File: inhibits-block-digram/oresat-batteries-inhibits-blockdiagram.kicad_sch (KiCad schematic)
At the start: 20 parts, among them J1 RBF, J2 RBF TAG, Q1 Q_NMOS, Q2 Q_PMOS, Q3 Q_PMOS, Q4 Q_PMOS, Q6 Q_PMOS, SW1 NEG BATTERY DISCONNECT, SW2 POSITIVE BATTERY DISCONNECT 1, SW3 POSITIVE BATT DISC 2, SW4 POSITIVE BATT DISC 3

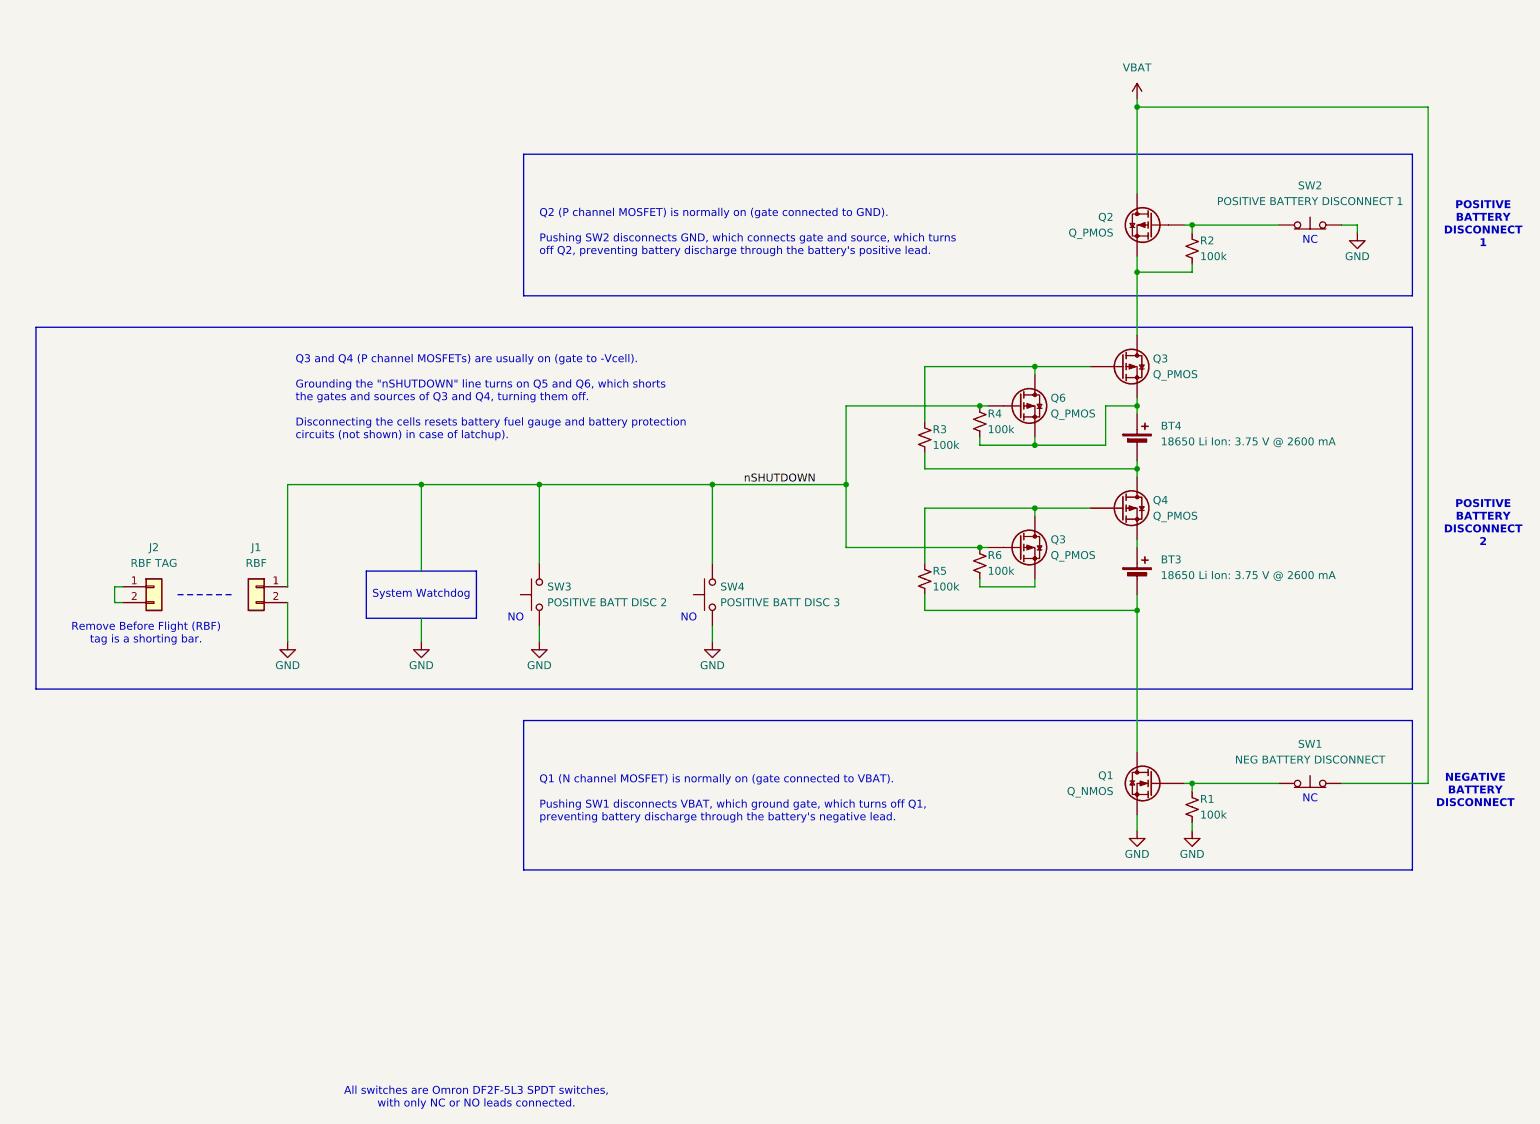
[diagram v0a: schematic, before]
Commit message: Revision 2.1 of the OreSat1 battery inhibits block diagram. Committing PDF for posterity
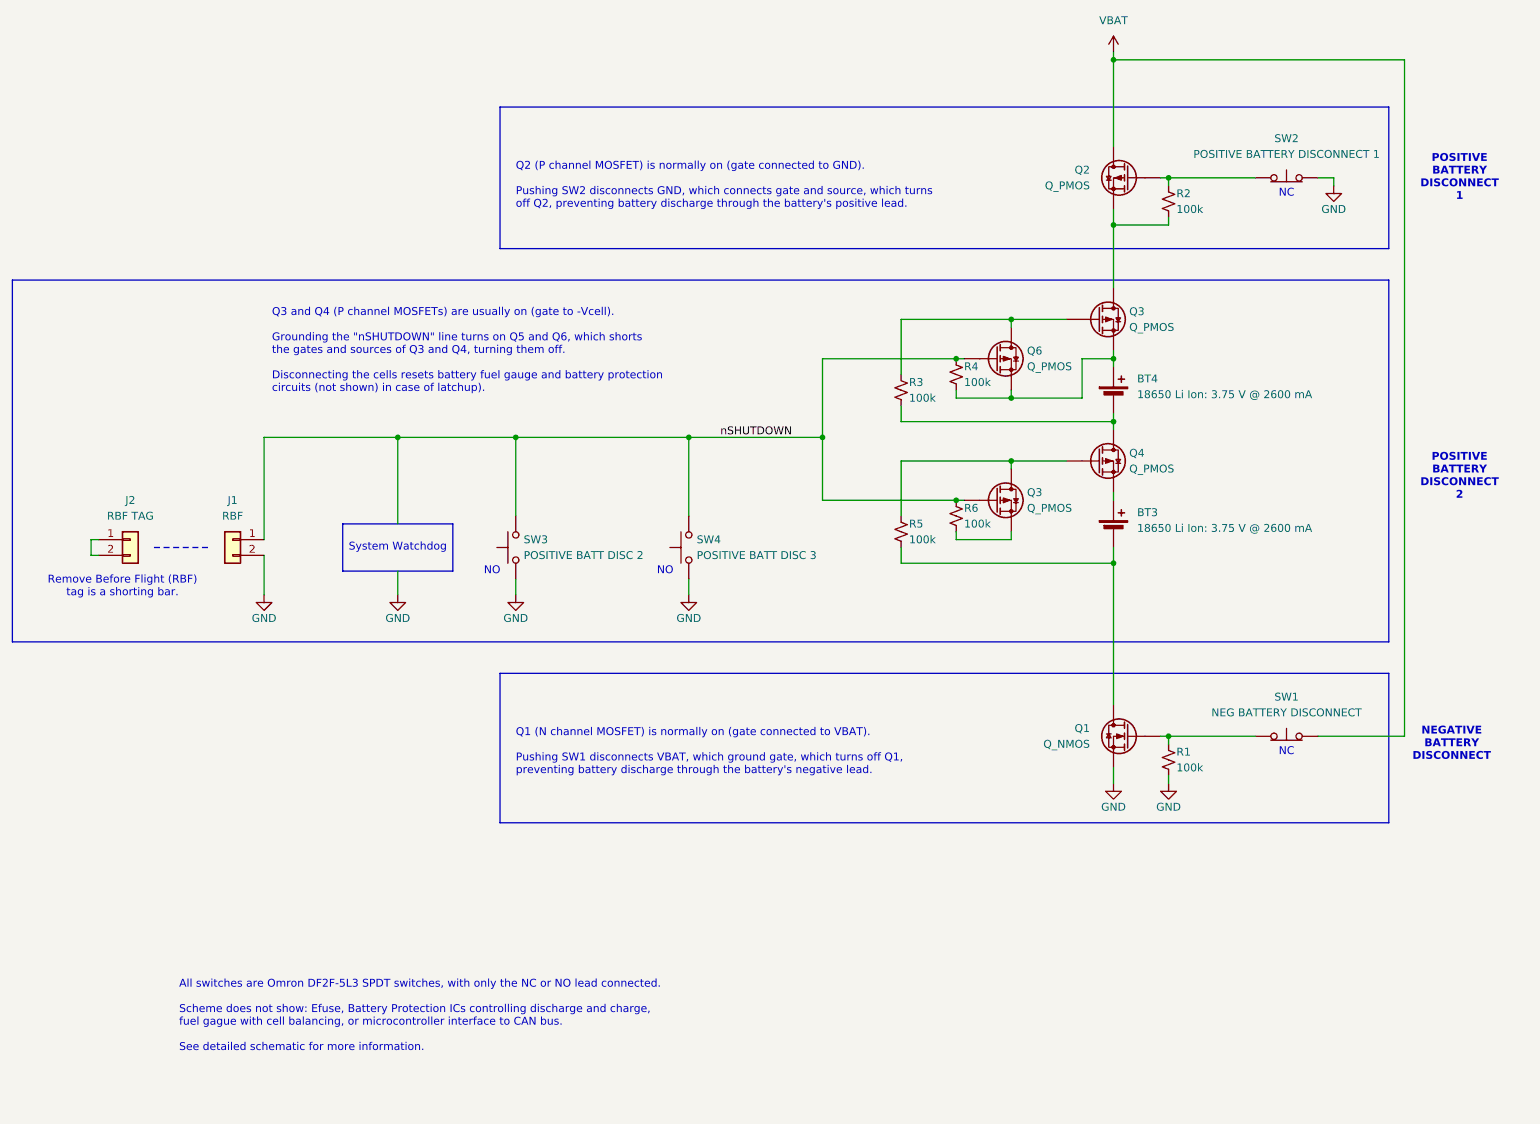
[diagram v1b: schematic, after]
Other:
- note added: "All switches are Omron DF2F-5L3 SPDT switches, with only the NC or NO lead connected. Scheme does not show: Efuse, Battery Protection ICs controlling discharge and charge, fuel gague with cell balancing, or microcontroller interface to CAN bus. See detailed schematic for more information."
- note removed: "All switches are Omron DF2F-5L3 SPDT switches, with only NC or NO leads connected."
- title: OreSat Power Inhibit Scheme -> OreSat Battery Inhibit Scheme
- moved on the sheet: BT3, BT4, J1, J2, Q1, Q2, Q3, Q4, Q6, R1, R2, R3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
